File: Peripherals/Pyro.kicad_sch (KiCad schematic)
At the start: 3 parts, among them Q3 IRFML8244TRPBF

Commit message: Reorganised repo
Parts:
- D5: value 1N4007 -> (none); footprint Diode_SMD:D_SOD-123 -> (none)
- Q3: value IRFML8244TRPBF -> (none); footprint Package_TO_SOT_SMD:SOT-23 -> (none)
- RN1: value 22k -> (none); footprint Resistor_SMD:R_Array_Convex_4x0603 -> (none)
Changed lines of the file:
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@@
     (effects (font (size 1.27 1.27)) (justify left))
-  )
-  (symbol (lib_id "Device:R_Pack04_Split") (at 109.22 50.8 180) (unit 2)
-    (in_bom yes) (on_board yes) (fields_autoplaced)
-    (property "Reference" "RN1" (id 0) (at 111.76 49.5299 0)
-      (effects (font (size 1.27 1.27)) (justify right))
-    )
-    (property "Value" "22k" (id 1) (at 111.76 52.0699 0)
-      (effects (font (size 1.27 1.27)) (justify right))
-    )
-    (property "Footprint" "Resistor_SMD:R_Array_Convex_4x0603" (id 2) (at 111.252 50.8 90)
-      (effects (font (size 1.27 1.27)) hide)
-    )
-    (property "Datasheet" "~" (id 3) (at 109.22 50.8 0)
-      (effects (font (size 1.27 1.27)) hide)
-    )
-    (pin "1")
-    (pin "8")
-    (pin "2")
-    (pin "7")
-    (pin "3")
-    (pin "6")
-    (pin "4")
-    (pin "5")
-  )
-  (symbol (lib_id "Device:R_Pack04_Split") (at 109.22 63.5 180) (unit 3)
-    (in_bom yes) (on_board yes) (fields_autoplaced)
-    (property "Reference" "RN1" (id 0) (at 111.76 62.2299 0)
-      (effects (font (size 1.27 1.27)) (justify right))
-    )
-    (property "Value" "22k" (id 1) (at 111.76 64.7699 0)
-      (effects (font (size 1.27 1.27)) (justify right))
-    )
-    (property "Footprint" "Resistor_SMD:R_Array_Convex_4x0603" (id 2) (at 111.252 63.5 90)
-      (effects (font (size 1.27 1.27)) hide)
-    )
-    (property "Datasheet" "~" (id 3) (at 109.22 63.5 0)
-      (effects (font (size 1.27 1.27)) hide)
-    )
-    (pin "1")
-    (pin "8")
-    (pin "2")
-    (pin "7")
-    (pin "3")
-    (pin "6")
-    (pin "4")
-    (pin "5")
-  )
-  (symbol (lib_id "power:GND") (at 100.33 82.55 0) (unit 1)
-    (in_bom yes) (on_board yes) (fields_autoplaced)
-    (property "Reference" "#PWR071" (id 0) (at 100.33 88.9 0)
-      (effects (font (size 1.27 1.27)) hide)
-    )
-    (property "Value" "GND" (id 1) (at 100.33 87.63 0))
-    (property "Footprint" "" (id 2) (at 100.33 82.55 0)
-      (effects (font (size 1.27 1.27)) hide)
-    )
-    (property "Datasheet" "" (id 3) (at 100.33 82.55 0)
-      (effects (font (size 1.27 1.27)) hide)
-    )
-    (pin "1")
-  )
-  (symbol (lib_id "Device:Q_NMOS_GDS") (at 97.79 67.31 0) (unit 1)
-    (in_bom yes) (on_board yes)
-    (property "Reference" "Q3" (id 0) (at 93.98 63.5 0))
-    (property "Value" "    IRFML8244TRPBF" (id 1) (at 85.09 69.85 0)
-      (effects (font (size 1.27 1.27)) hide)
-    )
-    (property "Footprint" "Package_TO_SOT_SMD:SOT-23" (id 2) (at 102.87 64.77 0)
-      (effects (font (size 1.27 1.27)) hide)
-    )
-    (property "Datasheet" "~" (id 3) (at 97.79 67.31 0)
-      (effects (font (size 1.27 1.27)) hide)
-    )
-    (pin "1")
-    (pin "2")
-    (pin "3")
-  )
-  (symbol (lib_id "Diode:1N914") (at 120.65 50.8 90) (mirror x) (unit 1)
-    (in_bom yes) (on_board yes)
-    (property "Reference" "D5" (id 0) (at 123.19 48.26 90))
-    (property "Value" "1N4007" (id 1) (at 125.73 53.34 90))
-    (property "Footprint" "Diode_SMD:D_SOD-123" (id 2) (at 125.095 50.8 0)
-      (effects (font (size 1.27 1.27)) hide)
-    )
-    (property "Datasheet" "http://www.vishay.com/docs/85622/1n914.pdf" (id 3) (at 120.65 50.8 0)
-      (effects (font (size 1.27 1.27)) hide)
-    )
-    (property "LCSC" "C727081" (id 4) (at 120.65 50.8 0)
-      (effects (font (size 1.27 1.27)) hide)
-    )
-    (property "JLC" "SOD-123FL" (id 5) (at 120.65 50.8 0)
-      (effects (font (size 1.27 1.27)) hide)
-    )
-    (pin "1")
-    (pin "2")
-  )
-  (symbol (lib_id "Device:R_Pack04_Split") (at 90.17 73.66 180) (unit 1)
-    (in_bom yes) (on_board yes) (fields_autoplaced)
-    (property "Reference" "RN1" (id 0) (at 92.71 72.3899 0)
-      (effects (font (size 1.27 1.27)) (justify right))
-    )
-    (property "Value" "22k" (id 1) (at 92.71 74.9299 0)
-      (effects (font (size 1.27 1.27)) (justify right))
-    )
-    (property "Footprint" "Resistor_SMD:R_Array_Convex_4x0603" (id 2) (at 92.202 73.66 90)
-      (effects (font (size 1.27 1.27)) hide)
-    )
-    (property "Datasheet" "~" (id 3) (at 90.17 73.66 0)
-      (effects (font (size 1.27 1.27)) hide)
-    )
-    (pin "1")
-    (pin "8")
-    (pin "2")
-    (pin "7")
-    (pin "3")
-    (pin "6")
-    (pin "4")
-    (pin "5")
   )
   (symbol (lib_id "Device:R_Pack04_Split") (at 109.22 73.66 180) (unit 4)
@@
       (effects (font (size 1.27 1.27)) (justify right))
     )
-    (property "Value" "22k" (id 1) (at 111.76 74.9299 0)
+    (property "Value" "" (id 1) (at 111.76 74.9299 0)
       (effects (font (size 1.27 1.27)) (justify right))
     )
-    (property "Footprint" "Resistor_SMD:R_Array_Convex_4x0603" (id 2) (at 111.252 73.66 90)
+    (property "Footprint" "" (id 2) (at 111.252 73.66 90)
       (effects (font (size 1.27 1.27)) hide)
     )
@@
       (effects (font (size 1.27 1.27)) hide)
     )
-    (property "Value" "+3V3" (id 1) (at 120.65 39.37 0))
+    (property "Value" "" (id 1) (at 120.65 39.37 0))
     (property "Footprint" "" (id 2) (at 120.65 44.45 0)
       (effects (font (size 1.27 1.27)) hide)
@@
     (pin "1")
   )
+  (symbol (lib_id "Diode:1N914") (at 120.65 50.8 90) (mirror x) (unit 1)
+    (in_bom yes) (on_board yes)
+    (property "Reference" "D5" (id 0) (at 123.19 48.26 90))
+    (property "Value" "" (id 1) (at 125.73 53.34 90))
+    (property "Footprint" "" (id 2) (at 125.095 50.8 0)
+      (effects (font (size 1.27 1.27)) hide)
+    )
+    (property "Datasheet" "http://www.vishay.com/docs/85622/1n914.pdf" (id 3) (at 120.65 50.8 0)
+      (effects (font (size 1.27 1.27)) hide)
+    )
+    (property "LCSC" "C727081" (id 4) (at 120.65 50.8 0)
+      (effects (font (size 1.27 1.27)) hide)
+    )
+    (property "JLC" "SOD-123FL" (id 5) (at 120.65 50.8 0)
+      (effects (font (size 1.27 1.27)) hide)
+    )
+    (pin "1")
+    (pin "2")
+  )
+  (symbol (lib_id "power:GND") (at 100.33 82.55 0) (unit 1)
+    (in_bom yes) (on_board yes) (fields_autoplaced)
+    (property "Reference" "#PWR071" (id 0) (at 100.33 88.9 0)
+      (effects (font (size 1.27 1.27)) hide)
+    )
+    (property "Value" "" (id 1) (at 100.33 87.63 0))
+    (property "Footprint" "" (id 2) (at 100.33 82.55 0)
+      (effects (font (size 1.27 1.27)) hide)
+    )
+    (property "Datasheet" "" (id 3) (at 100.33 82.55 0)
+      (effects (font (size 1.27 1.27)) hide)
+    )
+    (pin "1")
+  )
+  (symbol (lib_id "Device:R_Pack04_Split") (at 109.22 63.5 180) (unit 3)
+    (in_bom yes) (on_board yes) (fields_autoplaced)
+    (property "Reference" "RN1" (id 0) (at 111.76 62.2299 0)
+      (effects (font (size 1.27 1.27)) (justify right))
+    )
+    (property "Value" "" (id 1) (at 111.76 64.7699 0)
+      (effects (font (size 1.27 1.27)) (justify right))
+    )
+    (property "Footprint" "" (id 2) (at 111.252 63.5 90)
+      (effects (font (size 1.27 1.27)) hide)
+    )
+    (property "Datasheet" "~" (id 3) (at 109.22 63.5 0)
+      (effects (font (size 1.27 1.27)) hide)
+    )
+    (pin "1")
+    (pin "8")
+    (pin "2")
+    (pin "7")
+    (pin "3")
+    (pin "6")
+    (pin "4")
+    (pin "5")
+  )
+  (symbol (lib_id "Device:R_Pack04_Split") (at 109.22 50.8 180) (unit 2)
+    (in_bom yes) (on_board yes) (fields_autoplaced)
+    (property "Reference" "RN1" (id 0) (at 111.76 49.5299 0)
+      (effects (font (size 1.27 1.27)) (justify right))
+    )
+    (property "Value" "" (id 1) (at 111.76 52.0699 0)
+      (effects (font (size 1.27 1.27)) (justify right))
+    )
+    (property "Footprint" "" (id 2) (at 111.252 50.8 90)
+      (effects (font (size 1.27 1.27)) hide)
+    )
+    (property "Datasheet" "~" (id 3) (at 109.22 50.8 0)
+      (effects (font (size 1.27 1.27)) hide)
+    )
+    (pin "1")
+    (pin "8")
+    (pin "2")
+    (pin "7")
+    (pin "3")
+    (pin "6")
+    (pin "4")
+    (pin "5")
+  )
+  (symbol (lib_id "Device:R_Pack04_Split") (at 90.17 73.66 180) (unit 1)
+    (in_bom yes) (on_board yes) (fields_autoplaced)
+    (property "Reference" "RN1" (id 0) (at 92.71 72.3899 0)
+      (effects (font (size 1.27 1.27)) (justify right))
+    )
+    (property "Value" "" (id 1) (at 92.71 74.9299 0)
+      (effects (font (size 1.27 1.27)) (justify right))
+    )
+    (property "Footprint" "" (id 2) (at 92.202 73.66 90)
+      (effects (font (size 1.27 1.27)) hide)
+    )
+    (property "Datasheet" "~" (id 3) (at 90.17 73.66 0)
+      (effects (font (size 1.27 1.27)) hide)
+    )
+    (pin "1")
+    (pin "8")
+    (pin "2")
+    (pin "7")
+    (pin "3")
+    (pin "6")
+    (pin "4")
+    (pin "5")
+  )
+  (symbol (lib_id "Device:Q_NMOS_GDS") (at 97.79 67.31 0) (unit 1)
+    (in_bom yes) (on_board yes)
+    (property "Reference" "Q3" (id 0) (at 93.98 63.5 0))
+    (property "Value" "" (id 1) (at 85.09 69.85 0)
+      (effects (font (size 1.27 1.27)) hide)
+    )
+    (property "Footprint" "" (id 2) (at 102.87 64.77 0)
+      (effects (font (size 1.27 1.27)) hide)
+    )
+    (property "Datasheet" "~" (id 3) (at 97.79 67.31 0)
+      (effects (font (size 1.27 1.27)) hide)
+    )
+    (pin "1")
+    (pin "2")
+    (pin "3")
+  )
 )

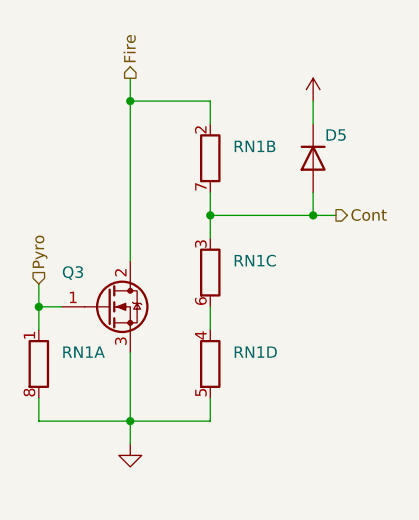
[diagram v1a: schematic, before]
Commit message: rev2 changes excluding pyro
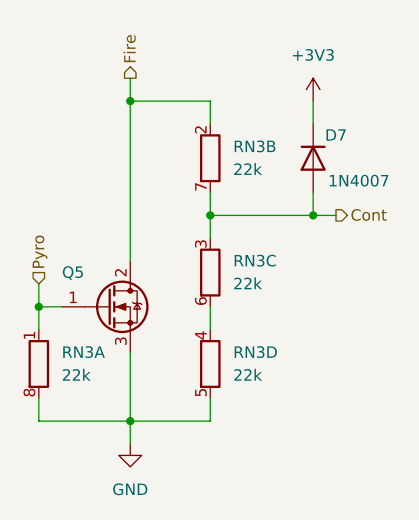
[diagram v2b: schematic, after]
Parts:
- D7: renamed from D5; value (none) -> 1N4007; footprint (none) -> Diode_SMD:D_SOD-123
- Q5: renamed from Q3; value (none) -> IRFML8244TRPBF; footprint (none) -> Package_TO_SOT_SMD:SOT-23
- RN3: renamed from RN1; value (none) -> 22k; footprint (none) -> Resistor_SMD:R_Array_Convex_4x0603
